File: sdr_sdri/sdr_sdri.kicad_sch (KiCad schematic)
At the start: 0 parts

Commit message: mengerti
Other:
- added sheet PowerSOC (PowerSOC.kicad_sch)
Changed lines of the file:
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@@
 (kicad_sch (version 20211123) (generator eeschema)
   (paper "A4")
+  (sheet (at 27.94 27.94) (size 27.94 15.24)
+    (stroke (width 0.1524) (type solid) (color 0 0 0 1))
+    (fill (color 254 255 102 1.0000))
+    (property "Sheet name" "PowerSOC" (id 0) (at 36.83 33.02 0)
+      (effects (font (size 1.27 1.27)) (justify left bottom))
+    )
+    (property "Sheet file" "PowerSOC.kicad_sch" (id 1) (at 29.21 39.37 0)
+      (effects (font (size 1.27 1.27)) (justify left top))
+    )
+  )
   (sheet_instances
     (path "/" (page "1"))
+    (path "/2b97c787-dfd5-484f-a9f0-4eb30c86ede3" (page "2"))
+  )
+  (symbol_instances
+    (path "/2b97c787-dfd5-484f-a9f0-4eb30c86ede3/0b76738c-4fb8-49b2-b36c-e9cd019d97e8"
+      (reference "C?") (unit 1) (value "470nF") (footprint "")
+    )
+    (path "/2b97c787-dfd5-484f-a9f0-4eb30c86ede3/1f64aabe-a74b-4627-bd6b-763591bcb6f0"
+      (reference "C?") (unit 1) (value "470nF") (footprint "")
+    )
+    (path "/2b97c787-dfd5-484f-a9f0-4eb30c86ede3/26f4d942-6186-4935-ba82-64435ee06d00"
+      (reference "C?") (unit 1) (value "470nF") (footprint "")
+    )
+    (path "/2b97c787-dfd5-484f-a9f0-4eb30c86ede3/277a56d2-3b03-49a8-84e0-a54f0ec056fc"
+      (reference "C?") (unit 1) (value "100uF") (footprint "")
+    )
+    (path "/2b97c787-dfd5-484f-a9f0-4eb30c86ede3/35eb36bf-1ba9-4fb4-bd1b-79b9f9ab6efc"
+      (reference "C?") (unit 1) (value "47uF") (footprint "")
+    )
+    (path "/2b97c787-dfd5-484f-a9f0-4eb30c86ede3/36237051-35e8-482d-8ba3-8ff77215832a"
+      (reference "C?") (unit 1) (value "100uF") (footprint "")
+    )
+    (path "/2b97c787-dfd5-484f-a9f0-4eb30c86ede3/41da1ee0-2558-49fa-b1be-35bc00a3d943"
+      (reference "C?") (unit 1) (value "100uF") (footprint "")
+    )
+    (path "/2b97c787-dfd5-484f-a9f0-4eb30c86ede3/57fab0cd-64d5-4709-aec1-f88c9f3e372e"
+      (reference "C?") (unit 1) (value "4.7uF") (footprint "")
+    )
+    (path "/2b97c787-dfd5-484f-a9f0-4eb30c86ede3/5dfbd24d-dd64-4076-89a0-bc955d0eaeb6"
+      (reference "C?") (unit 1) (value "470nF") (footprint "")
+    )
+    (path "/2b97c787-dfd5-484f-a9f0-4eb30c86ede3/6248309e-c258-4f25-be2f-52feedbe4e84"
+      (reference "C?") (unit 1) (value "470nF") (footprint "")
+    )
+    (path "/2b97c787-dfd5-484f-a9f0-4eb30c86ede3/65737b64-3dbf-4526-b3f0-454c4e70e7e4"
+      (reference "C?") (unit 1) (value "470nF") (footprint "")
+    )
+    (path "/2b97c787-dfd5-484f-a9f0-4eb30c86ede3/68d1afd5-d04e-4faa-a6b6-eaee2af62176"
+      (reference "C?") (unit 1) (value "470nF") (footprint "")
+    )
+    (path "/2b97c787-dfd5-484f-a9f0-4eb30c86ede3/733e9e86-e498-4455-b83c-801d1a75cb35"
+      (reference "C?") (unit 1) (value "4.7uF") (footprint "")
+    )
+    (path "/2b97c787-dfd5-484f-a9f0-4eb30c86ede3/85151899-f980-49c3-ba0e-aefc2d155ebd"
+      (reference "C?") (unit 1) (value "470nF") (footprint "")
+    )
+    (path "/2b97c787-dfd5-484f-a9f0-4eb30c86ede3/8c49ec00-e85d-4e8e-9a76-fdc175605236"
+      (reference "C?") (unit 1) (value "470nF") (footprint "")
+    )
+    (path "/2b97c787-dfd5-484f-a9f0-4eb30c86ede3/8ea22bda-b9de-43ec-9043-ba05ee5180fe"
+      (reference "C?") (unit 1) (value "470nF") (footprint "")
+    )
+    (path "/2b97c787-dfd5-484f-a9f0-4eb30c86ede3/935dffbe-7cb3-4aa2-b49f-3972307b8aa4"
+      (reference "C?") (unit 1) (value "4.7uF") (footprint "")
+    )
+    (path "/2b97c787-dfd5-484f-a9f0-4eb30c86ede3/9a7f8d7f-7282-4b83-b968-c2378197f4cc"
+      (reference "C?") (unit 1) (value "4.7uF") (footprint "")
+    )
+    (path "/2b97c787-dfd5-484f-a9f0-4eb30c86ede3/a7f8195b-d025-4858-b88c-4a73789651f6"
+      (reference "C?") (unit 1) (value "4.7uF") (footprint "")
+    )
+    (path "/2b97c787-dfd5-484f-a9f0-4eb30c86ede3/b4a24ee9-0043-435d-9912-7086ae977da6"
+      (reference "C?") (unit 1) (value "470nF") (footprint "")
+    )
+    (path "/2b97c787-dfd5-484f-a9f0-4eb30c86ede3/bdb65845-aab2-4c64-8089-818dc3ed3e68"
+      (reference "C?") (unit 1) (value "4.7uF") (footprint "")
+    )
+    (path "/2b97c787-dfd5-484f-a9f0-4eb30c86ede3/ca748d9b-da2e-4ff5-b204-89b746be22f8"
+      (reference "C?") (unit 1) (value "470nF") (footprint "")
+    )
+    (path "/2b97c787-dfd5-484f-a9f0-4eb30c86ede3/cc62458c-27cc-437b-beb0-b860f6ab0fae"
+      (reference "C?") (unit 1) (value "4.7uF") (footprint "")
+    )
+    (path "/2b97c787-dfd5-484f-a9f0-4eb30c86ede3/cd522734-cf91-433f-85bb-f0cdacfb0c9b"
+      (reference "C?") (unit 1) (value "4.7uF") (footprint "")
+    )
+    (path "/2b97c787-dfd5-484f-a9f0-4eb30c86ede3/d26ba5ba-67ea-4a69-8b1d-7f64534f5342"
+      (reference "C?") (unit 1) (value "470nF") (footprint "")
+    )
+    (path "/2b97c787-dfd5-484f-a9f0-4eb30c86ede3/dbbb015f-03ee-4a32-b294-a4269ec172ec"
+      (reference "C?") (unit 1) (value "470nF") (footprint "")
+    )
+    (path "/2b97c787-dfd5-484f-a9f0-4eb30c86ede3/f1cfdeca-75e7-4a11-8527-89b9f1942ffd"
+      (reference "C?") (unit 1) (value "470nF") (footprint "")
+    )
+    (path "/2b97c787-dfd5-484f-a9f0-4eb30c86ede3/f1f56aa4-07ad-43fe-b4e4-46a3a999d0bc"
+      (reference "C?") (unit 1) (value "4.7uF") (footprint "")
+    )
+    (path "/2b97c787-dfd5-484f-a9f0-4eb30c86ede3/f26bf2d0-ff2b-47e7-91ac-8ee09e12ba41"
+      (reference "C?") (unit 1) (value "4.7uF") (footprint "")
+    )
+    (path "/2b97c787-dfd5-484f-a9f0-4eb30c86ede3/331a683f-daa9-49bd-a0a9-70c8218d3871"
+      (reference "U?") (unit 8) (value "Zynq-7010_7020") (footprint "")
+    )
   )
 )

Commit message: mer
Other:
- added sheet DDR_ext (DDR.kicad_sch)

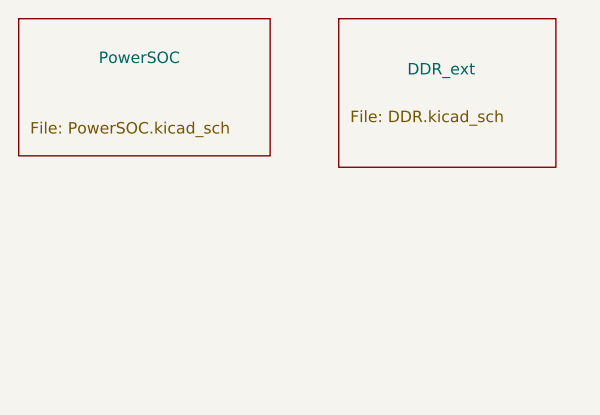
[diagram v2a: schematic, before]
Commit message: add ddr device
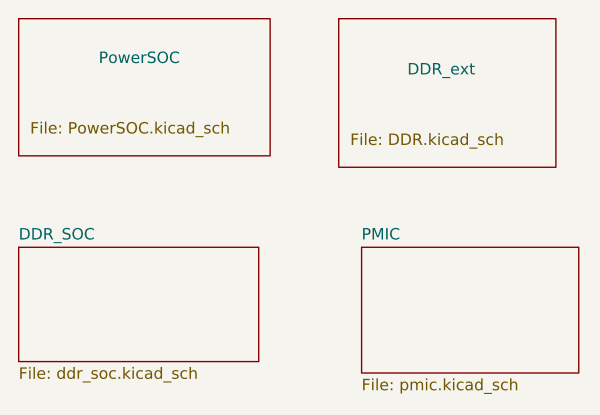
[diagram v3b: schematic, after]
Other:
- added sheet DDR_SOC (ddr_soc.kicad_sch)
- added sheet PMIC (pmic.kicad_sch)

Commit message: menambahkan connecsi k
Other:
- added sheet Bank500 (Bank500.kicad_sch)
- added sheet interfes (interfes.kicad_sch)
- added sheet osilator (osilator.kicad_sch)
